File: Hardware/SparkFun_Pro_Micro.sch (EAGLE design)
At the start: 43 parts, among them J2 Qwiic, U1 3.3V, U3 ATmega32U4, Y2 32MHz

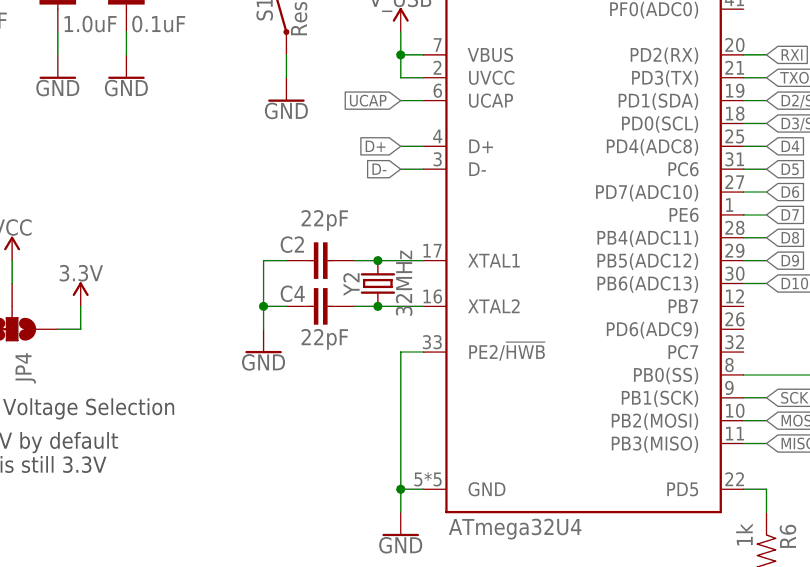
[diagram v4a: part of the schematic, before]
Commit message: Udpate xtal to 16MHz
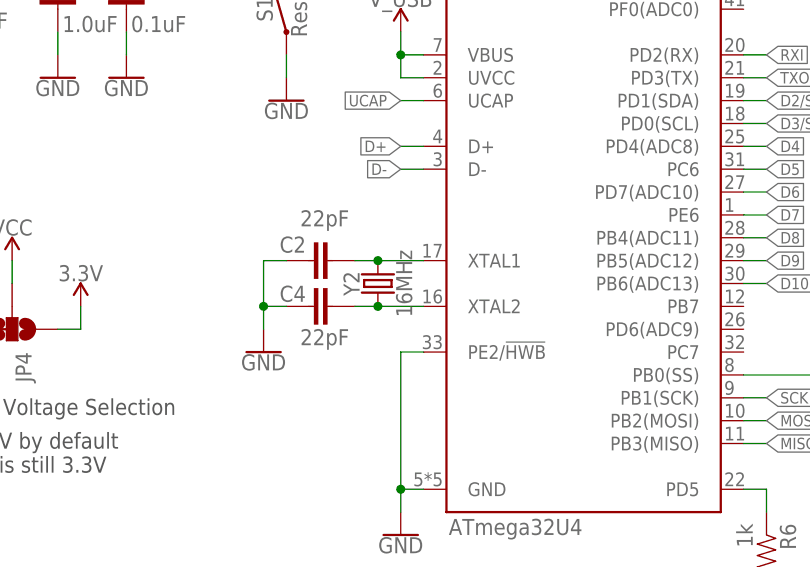
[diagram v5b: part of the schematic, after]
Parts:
- Y2: value 32MHz -> 16MHz; device SparkFun-Clocks:CRYSTAL-32MHZ-SMD-2.0X1.6MM -> SparkFun-Clocks:CRYSTAL-16MHZSMD-2X1.6
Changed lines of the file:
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@@
 <?xml version="1.0" encoding="utf-8"?>
 <!DOCTYPE eagle SYSTEM "eagle.dtd">
-<eagle version="9.5.1">
+<eagle version="9.5.2">
 <drawing>
 <settings>
@@
 <part name="SUPPLY7" library="SparkFun-PowerSymbols" deviceset="V_USB" device=""/>
 <part name="SUPPLY8" library="SparkFun-PowerSymbols" deviceset="V_USB" device=""/>
-<part name="Y2" library="SparkFun-Clocks" deviceset="CRYSTAL-32MHZ" device="-SMD-2.0X1.6MM" value="32MHz"/>
+<part name="Y2" library="SparkFun-Clocks" deviceset="CRYSTAL-16MHZ" device="SMD-2X1.6" value="16MHz"/>
 <part name="J2" library="SparkFun-Connectors" deviceset="QWIIC_CONNECTOR" device="JS-1MM" value="Qwiic"/>
 <part name="SUPPLY9" library="SparkFun-PowerSymbols" deviceset="V_USB" device=""/>

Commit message: Correct prodID on 22 ohm resistors.
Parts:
- R8, R9: device SparkFun-Resistors:22OHM-0402T-1/16W-1% -> SparkFun-Resistors:22OHM-0402-1/10W-1%
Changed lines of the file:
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@@
 <part name="J2" library="SparkFun-Connectors" deviceset="QWIIC_CONNECTOR" device="JS-1MM" value="Qwiic"/>
 <part name="SUPPLY9" library="SparkFun-PowerSymbols" deviceset="V_USB" device=""/>
-<part name="R8" library="SparkFun-Resistors" deviceset="22OHM" device="-0402T-1/16W-1%" value="22"/>
-<part name="R9" library="SparkFun-Resistors" deviceset="22OHM" device="-0402T-1/16W-1%" value="22"/>
+<part name="R8" library="SparkFun-Resistors" deviceset="22OHM" device="-0402-1/10W-1%" value="22"/>
+<part name="R9" library="SparkFun-Resistors" deviceset="22OHM" device="-0402-1/10W-1%" value="22"/>
 <part name="GND16" library="SparkFun-PowerSymbols" deviceset="GND" device=""/>
 <part name="LOGO2" library="SparkFun-Aesthetics" deviceset="QWIIC_LOGO" device="_4MM"/>

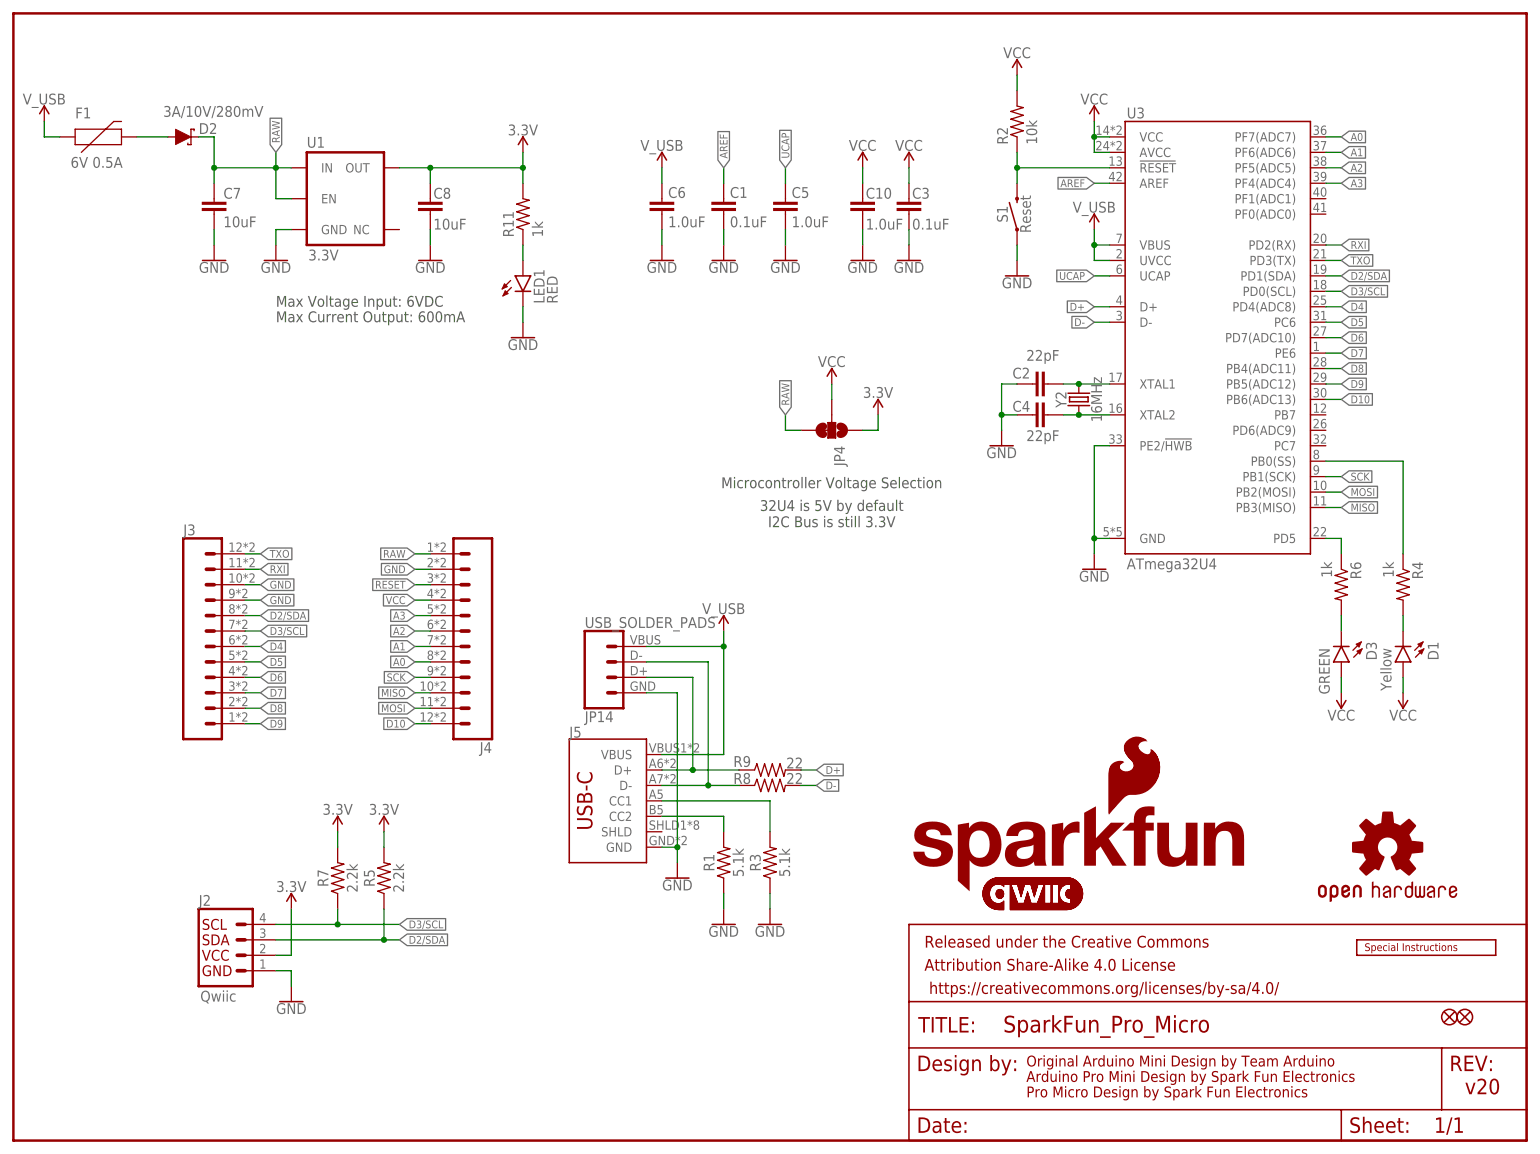
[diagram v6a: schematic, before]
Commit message: fixing paste issue
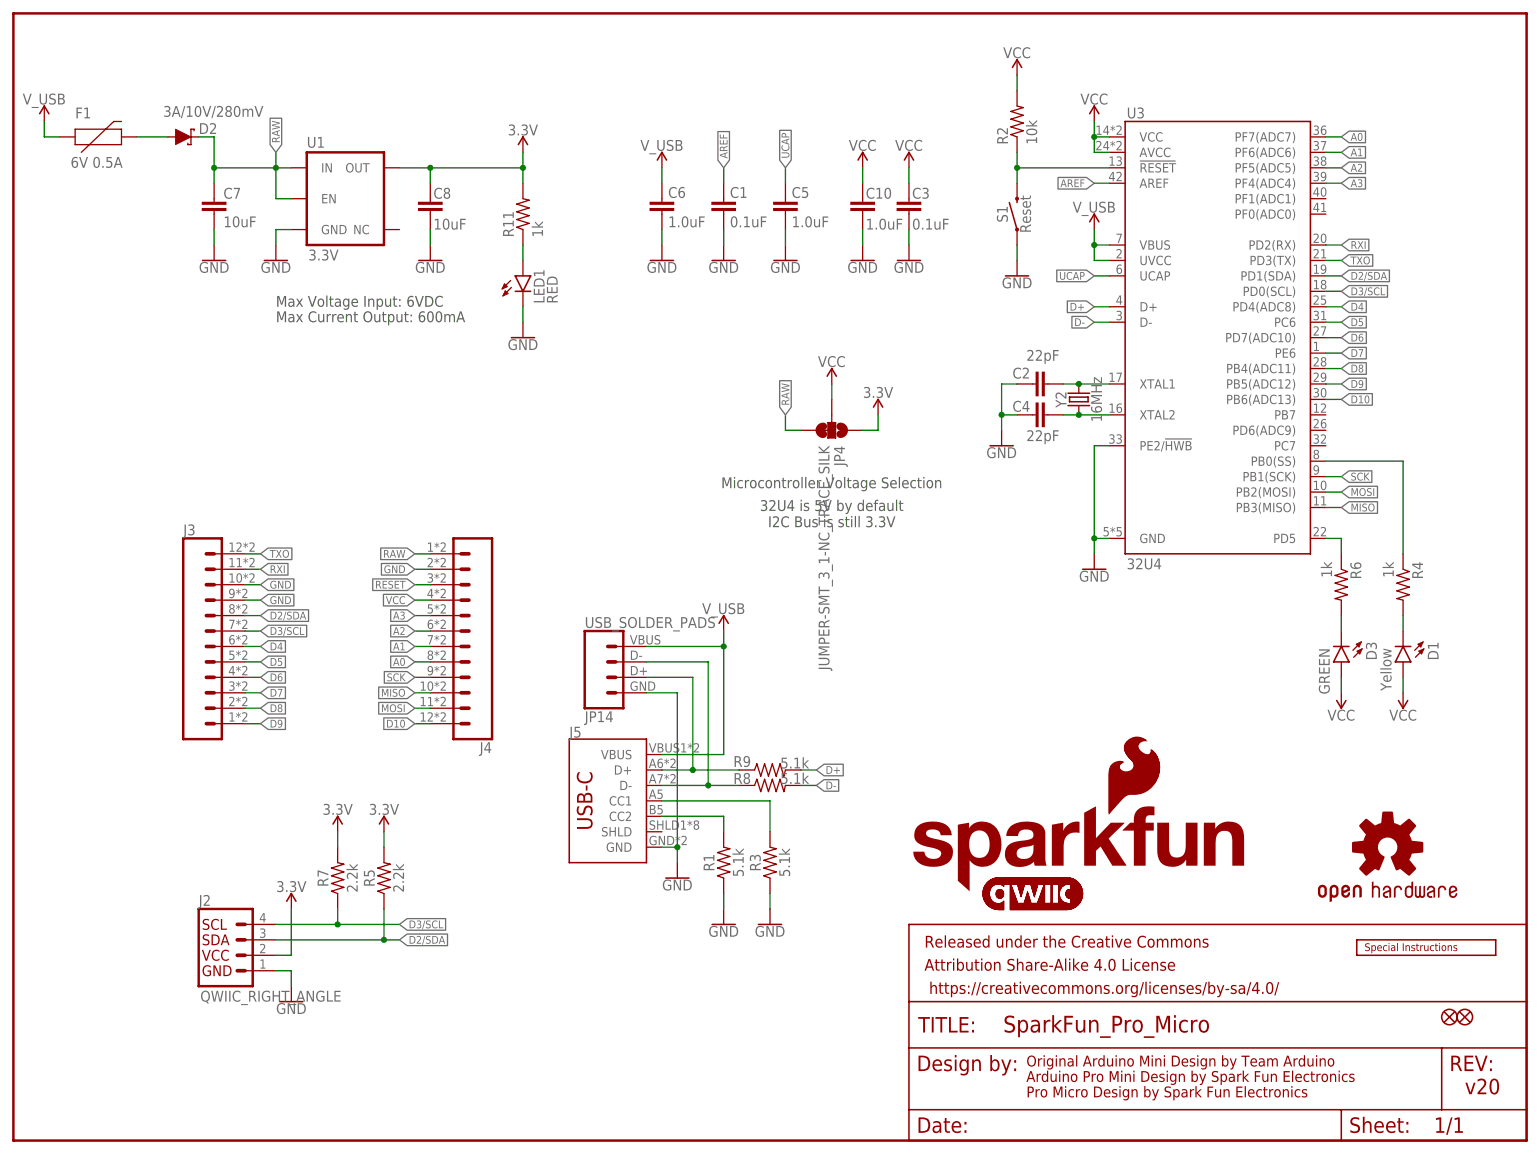
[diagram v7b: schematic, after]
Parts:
- J2: value Qwiic -> QWIIC_RIGHT_ANGLE
- R8, R9: value 22 -> 5.1k; device SparkFun-Resistors:22OHM-0402-1/10W-1% -> SparkFun-Resistors:5.1KOHM-0402T-1/16W-1%
- U3: value ATmega32U4 -> 32U4; device SparkFun-IC-Microcontroller:ATMEGA32U41:1 -> SparkFun-IC-Microcontroller:ATMEGA32U41:1-LESS_PASTE
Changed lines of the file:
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@@
 <drawing>
 <settings>
-<setting alwaysvectorfont="yes"/>
+<setting alwaysvectorfont="no"/>
 <setting keepoldvectorfont="yes"/>
 <setting verticaltext="up"/>
@@
 <part name="D3" library="SparkFun-LED" deviceset="LED-GREEN" device="0603" value="GREEN"/>
 <part name="U$3" library="SparkFun-Aesthetics" deviceset="OSHW-LOGO" device="MINI"/>
-<part name="U3" library="SparkFun-IC-Microcontroller" deviceset="ATMEGA32U4" device="1:1" value="ATmega32U4"/>
+<part name="U3" library="SparkFun-IC-Microcontroller" deviceset="ATMEGA32U4" device="1:1-LESS_PASTE" value="32U4"/>
 <part name="C2" library="SparkFun-Capacitors" deviceset="22PF" device="-0402T-16V-10%" value="22pF"/>
 <part name="C4" library="SparkFun-Capacitors" deviceset="22PF" device="-0402T-16V-10%" value="22pF"/>
@@
 <part name="SUPPLY8" library="SparkFun-PowerSymbols" deviceset="V_USB" device=""/>
 <part name="Y2" library="SparkFun-Clocks" deviceset="CRYSTAL-16MHZ" device="SMD-2X1.6" value="16MHz"/>
-<part name="J2" library="SparkFun-Connectors" deviceset="QWIIC_CONNECTOR" device="JS-1MM" value="Qwiic"/>
+<part name="J2" library="SparkFun-Connectors" deviceset="QWIIC_CONNECTOR" device="JS-1MM" value="QWIIC_RIGHT_ANGLE"/>
 <part name="SUPPLY9" library="SparkFun-PowerSymbols" deviceset="V_USB" device=""/>
-<part name="R8" library="SparkFun-Resistors" deviceset="22OHM" device="-0402-1/10W-1%" value="22"/>
-<part name="R9" library="SparkFun-Resistors" deviceset="22OHM" device="-0402-1/10W-1%" value="22"/>
+<part name="R8" library="SparkFun-Resistors" deviceset="5.1KOHM" device="-0402T-1/16W-1%" value="5.1k"/>
+<part name="R9" library="SparkFun-Resistors" deviceset="5.1KOHM" device="-0402T-1/16W-1%" value="5.1k"/>
 <part name="GND16" library="SparkFun-PowerSymbols" deviceset="GND" device=""/>
 <part name="LOGO2" library="SparkFun-Aesthetics" deviceset="QWIIC_LOGO" device="_4MM"/>
@@
 <part name="JP14" library="SparkFun-Connectors" deviceset="USB_SOLDER_PADS" device=""/>
 <part name="LOGO4" library="SparkFun-Aesthetics" deviceset="SFE_LOGO_FLAME" device=".1_INCH"/>
-<part name="JP4" library="SparkFun-Jumpers" deviceset="JUMPER-SMT_3_1-NC_TRACE" device="_SILK" value=""/>
+<part name="JP4" library="SparkFun-Jumpers" deviceset="JUMPER-SMT_3_1-NC_TRACE" device="_SILK" package3d_urn="urn:adsk.eagle:package:39288/1" value="JUMPER-SMT_3_1-NC_TRACE_SILK"/>
 <part name="J5" library="USBC" deviceset="USB_C" device="5"/>
 <part name="FRAME1" library="SparkFun-Aesthetics" deviceset="FRAME-LETTER" device=""/>
@@
 <attribute name="VALUE" x="116.84" y="86.614" size="1.778" layer="96" align="bottom-center"/>
 </instance>
-<instance part="R8" gate="G$1" x="124.46" y="58.42" smashed="yes">
+<instance part="R8" gate="R1" x="124.46" y="58.42" smashed="yes">
 <attribute name="NAME" x="119.888" y="58.674" size="1.778" layer="95" font="vector" align="bottom-center"/>
 <attribute name="VALUE" x="128.524" y="58.674" size="1.778" layer="96" font="vector" rot="R180" align="top-center"/>
 </instance>
-<instance part="R9" gate="G$1" x="124.46" y="60.96" smashed="yes">
+<instance part="R9" gate="R1" x="124.46" y="60.96" smashed="yes">
 <attribute name="NAME" x="119.888" y="61.468" size="1.778" layer="95" font="vector" align="bottom-center"/>
 <attribute name="VALUE" x="128.524" y="61.214" size="1.778" layer="96" font="vector" rot="R180" align="top-center"/>
@@
 <wire x1="129.54" y1="58.42" x2="132.08" y2="58.42" width="0.1524" layer="91"/>
 <label x="132.08" y="58.42" size="1.27" layer="95" xref="yes"/>
-<pinref part="R8" gate="G$1" pin="2"/>
+<pinref part="R8" gate="R1" pin="2"/>
 </segment>
 </net>
@@
 <wire x1="129.54" y1="60.96" x2="132.08" y2="60.96" width="0.1524" layer="91"/>
 <label x="132.08" y="60.96" size="1.27" layer="95" xref="yes"/>
-<pinref part="R9" gate="G$1" pin="2"/>
+<pinref part="R9" gate="R1" pin="2"/>
 </segment>
 </net>
@@
 <segment>
 <wire x1="106.68" y1="58.42" x2="114.3" y2="58.42" width="0.1524" layer="91"/>
-<pinref part="R8" gate="G$1" pin="1"/>
+<pinref part="R8" gate="R1" pin="1"/>
 <pinref part="JP14" gate="JP1" pin="2"/>
 <wire x1="114.3" y1="58.42" x2="119.38" y2="58.42" width="0.1524" layer="91"/>
@@
 <segment>
 <wire x1="106.68" y1="60.96" x2="111.76" y2="60.96" width="0.1524" layer="91"/>
-<pinref part="R9" gate="G$1" pin="1"/>
+<pinref part="R9" gate="R1" pin="1"/>
 <pinref part="JP14" gate="JP1" pin="3"/>
 <wire x1="111.76" y1="60.96" x2="119.38" y2="60.96" width="0.1524" layer="91"/>
@@
 which will not be processed correctly with this version.
 </note>
+<note version="8.3" severity="warning">
+Since Version 8.3, EAGLE supports URNs for individual library
+assets (packages, symbols, and devices). The URNs of those assets
+will not be understood (or retained) with this version.
+</note>
+<note version="8.3" severity="warning">
+Since Version 8.3, EAGLE supports the association of 3D packages
+with devices in libraries, schematics, and board files. Those 3D
+packages will not be understood (or retained) with this version.
+</note>
 </compatibility>

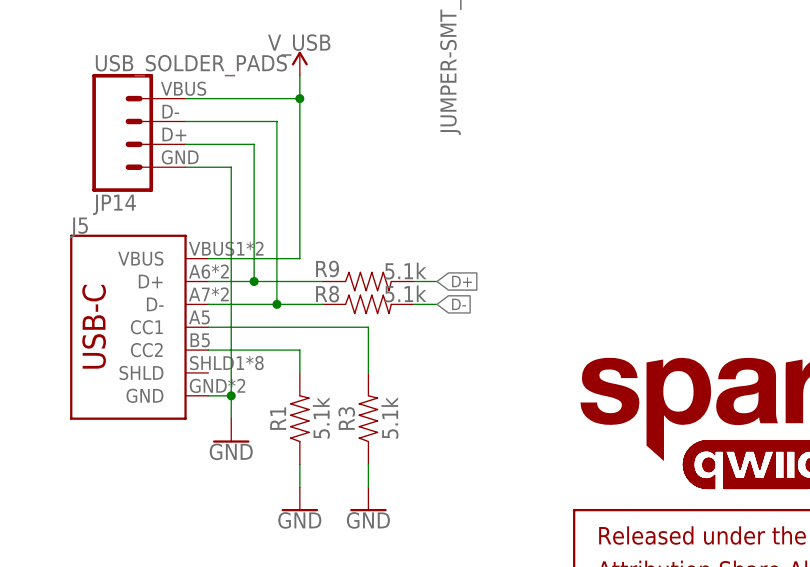
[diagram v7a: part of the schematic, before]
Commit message: changing PROD_ID on series D+/D- resistor to proper PROD_ID
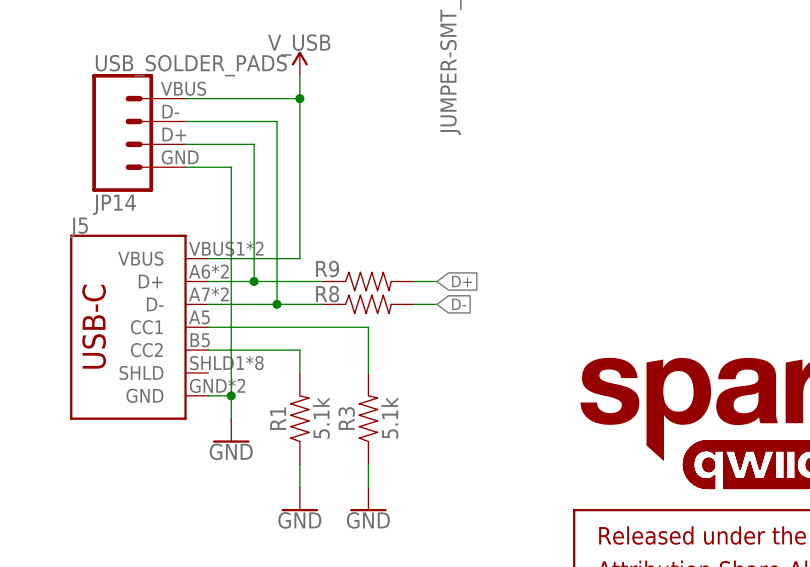
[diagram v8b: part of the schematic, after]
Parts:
- R8, R9: value 5.1k -> 22OHM-0402T-1/16W-1%; device SparkFun-Resistors:5.1KOHM-0402T-1/16W-1% -> SparkFun-Resistors:22OHM-0402T-1/16W-1%
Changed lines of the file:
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@@
 <part name="J2" library="SparkFun-Connectors" deviceset="QWIIC_CONNECTOR" device="JS-1MM" value="QWIIC_RIGHT_ANGLE"/>
 <part name="SUPPLY9" library="SparkFun-PowerSymbols" deviceset="V_USB" device=""/>
-<part name="R8" library="SparkFun-Resistors" deviceset="5.1KOHM" device="-0402T-1/16W-1%" value="5.1k"/>
-<part name="R9" library="SparkFun-Resistors" deviceset="5.1KOHM" device="-0402T-1/16W-1%" value="5.1k"/>
+<part name="R8" library="SparkFun-Resistors" deviceset="22OHM" device="-0402T-1/16W-1%" value="22OHM-0402T-1/16W-1%"/>
+<part name="R9" library="SparkFun-Resistors" deviceset="22OHM" device="-0402T-1/16W-1%" value="22OHM-0402T-1/16W-1%"/>
 <part name="GND16" library="SparkFun-PowerSymbols" deviceset="GND" device=""/>
 <part name="LOGO2" library="SparkFun-Aesthetics" deviceset="QWIIC_LOGO" device="_4MM"/>
@@
 <attribute name="VALUE" x="116.84" y="86.614" size="1.778" layer="96" align="bottom-center"/>
 </instance>
-<instance part="R8" gate="R1" x="124.46" y="58.42" smashed="yes">
+<instance part="R8" gate="G$1" x="124.46" y="58.42" smashed="yes">
 <attribute name="NAME" x="119.888" y="58.674" size="1.778" layer="95" font="vector" align="bottom-center"/>
-<attribute name="VALUE" x="128.524" y="58.674" size="1.778" layer="96" font="vector" rot="R180" align="top-center"/>
-</instance>
-<instance part="R9" gate="R1" x="124.46" y="60.96" smashed="yes">
+</instance>
+<instance part="R9" gate="G$1" x="124.46" y="60.96" smashed="yes">
 <attribute name="NAME" x="119.888" y="61.468" size="1.778" layer="95" font="vector" align="bottom-center"/>
-<attribute name="VALUE" x="128.524" y="61.214" size="1.778" layer="96" font="vector" rot="R180" align="top-center"/>
 </instance>
 <instance part="GND16" gate="1" x="45.72" y="22.86" smashed="yes">
@@
 <wire x1="129.54" y1="58.42" x2="132.08" y2="58.42" width="0.1524" layer="91"/>
 <label x="132.08" y="58.42" size="1.27" layer="95" xref="yes"/>
-<pinref part="R8" gate="R1" pin="2"/>
+<pinref part="R8" gate="G$1" pin="2"/>
 </segment>
 </net>
@@
 <wire x1="129.54" y1="60.96" x2="132.08" y2="60.96" width="0.1524" layer="91"/>
 <label x="132.08" y="60.96" size="1.27" layer="95" xref="yes"/>
-<pinref part="R9" gate="R1" pin="2"/>
+<pinref part="R9" gate="G$1" pin="2"/>
 </segment>
 </net>
@@
 <segment>
 <wire x1="106.68" y1="58.42" x2="114.3" y2="58.42" width="0.1524" layer="91"/>
-<pinref part="R8" gate="R1" pin="1"/>
+<pinref part="R8" gate="G$1" pin="1"/>
 <pinref part="JP14" gate="JP1" pin="2"/>
 <wire x1="114.3" y1="58.42" x2="119.38" y2="58.42" width="0.1524" layer="91"/>
@@
 <segment>
 <wire x1="106.68" y1="60.96" x2="111.76" y2="60.96" width="0.1524" layer="91"/>
-<pinref part="R9" gate="R1" pin="1"/>
+<pinref part="R9" gate="G$1" pin="1"/>
 <pinref part="JP14" gate="JP1" pin="3"/>
 <wire x1="111.76" y1="60.96" x2="119.38" y2="60.96" width="0.1524" layer="91"/>
